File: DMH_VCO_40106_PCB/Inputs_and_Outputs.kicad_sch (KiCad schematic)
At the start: 9 parts, among them J1 Sync, J2 V/Oct, J3 Exp FM, J4 Lin FM, J5 PW Mod, J6 Senoid, J7 Triangle, J8 Square, J9 Sawtooth

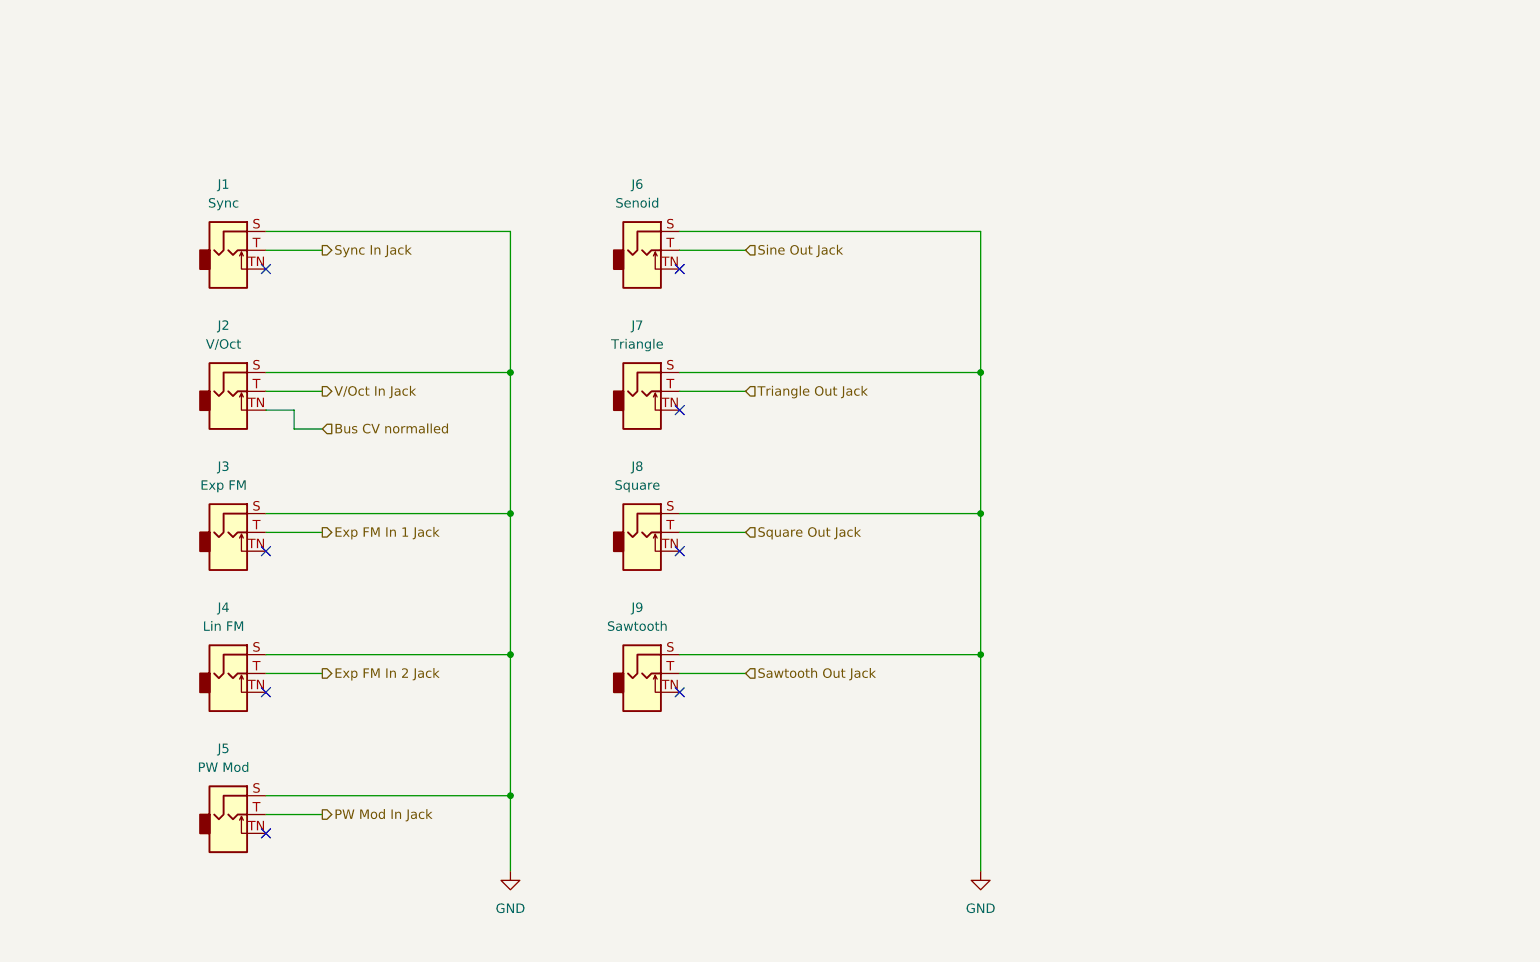
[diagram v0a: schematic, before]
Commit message: Added Sync and Bus CV switches
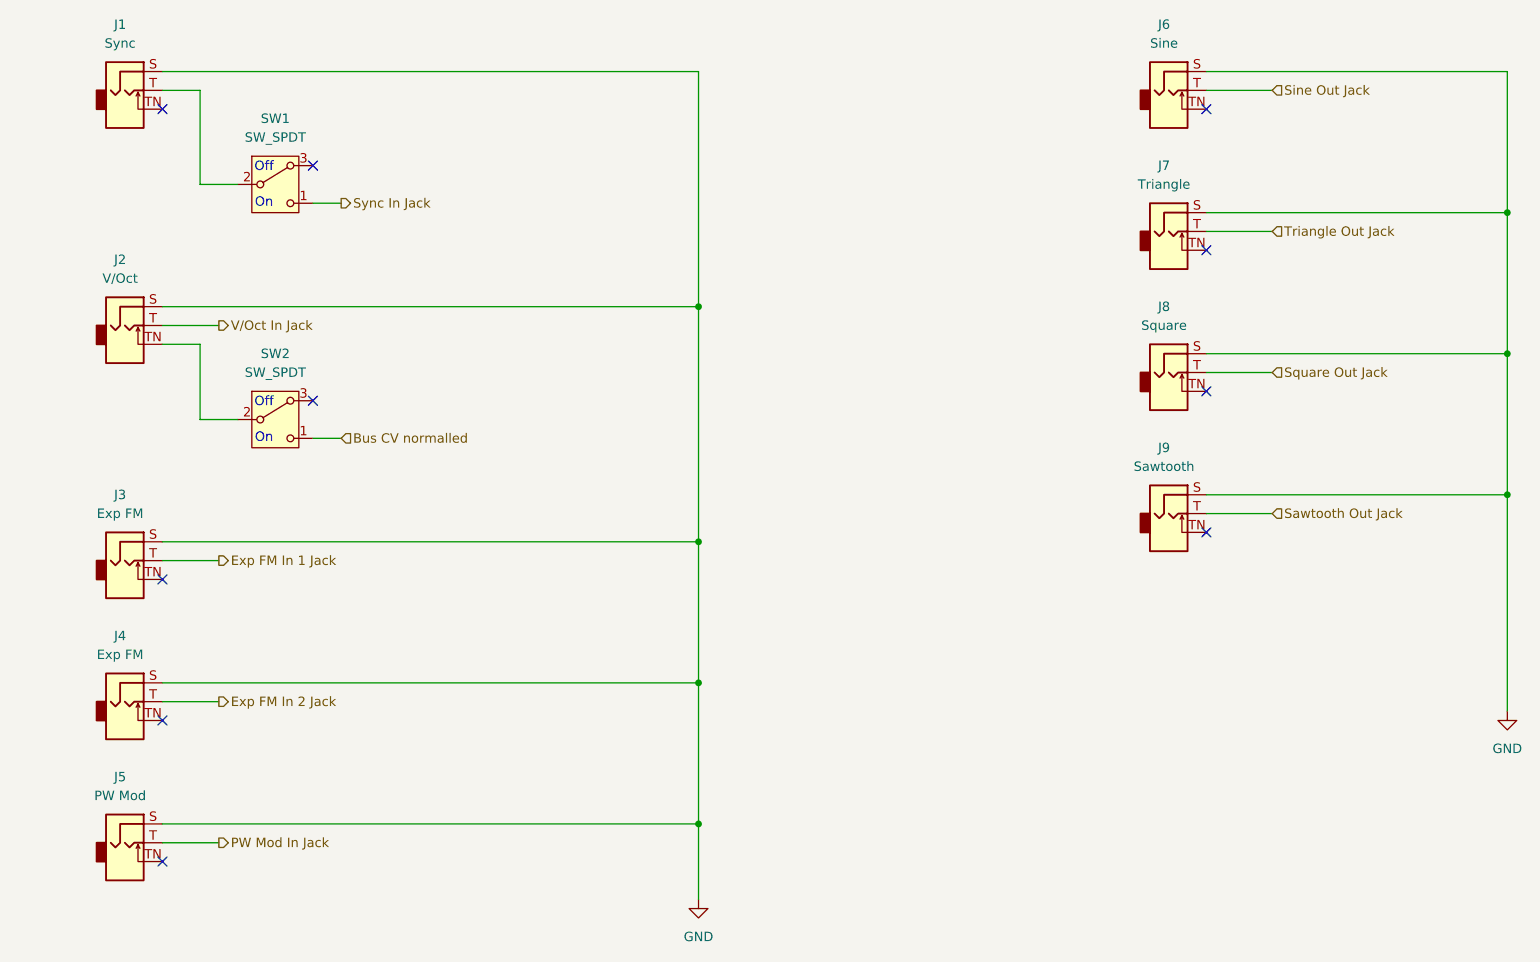
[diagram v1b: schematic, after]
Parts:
- added SW1, SW2: SW_SPDT, symbol Switch:SW_SPDT_321
- J4: value Lin FM -> Exp FM
- J6: value Senoid -> Sine
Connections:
- net Bus CV normalled: now also SW2.1 (C); no longer J2.TN
- net Sync In Jack: now also SW1.1 (C); no longer J1.T
- new net: J1.T, SW1.2 (B)
- new net: J2.TN, SW2.2 (B)
- no-connect marks 8 -> 10
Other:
- note added: "Off"
- note added: "On"
- moved on the sheet: J1, J2, J3, J4, J5, J6, J7, J8, J9

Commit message: Updated Tuner
- Changed uC to ATtiny4313
- Added LEDs
- Created "function" field and updated all jacks, switches and pots
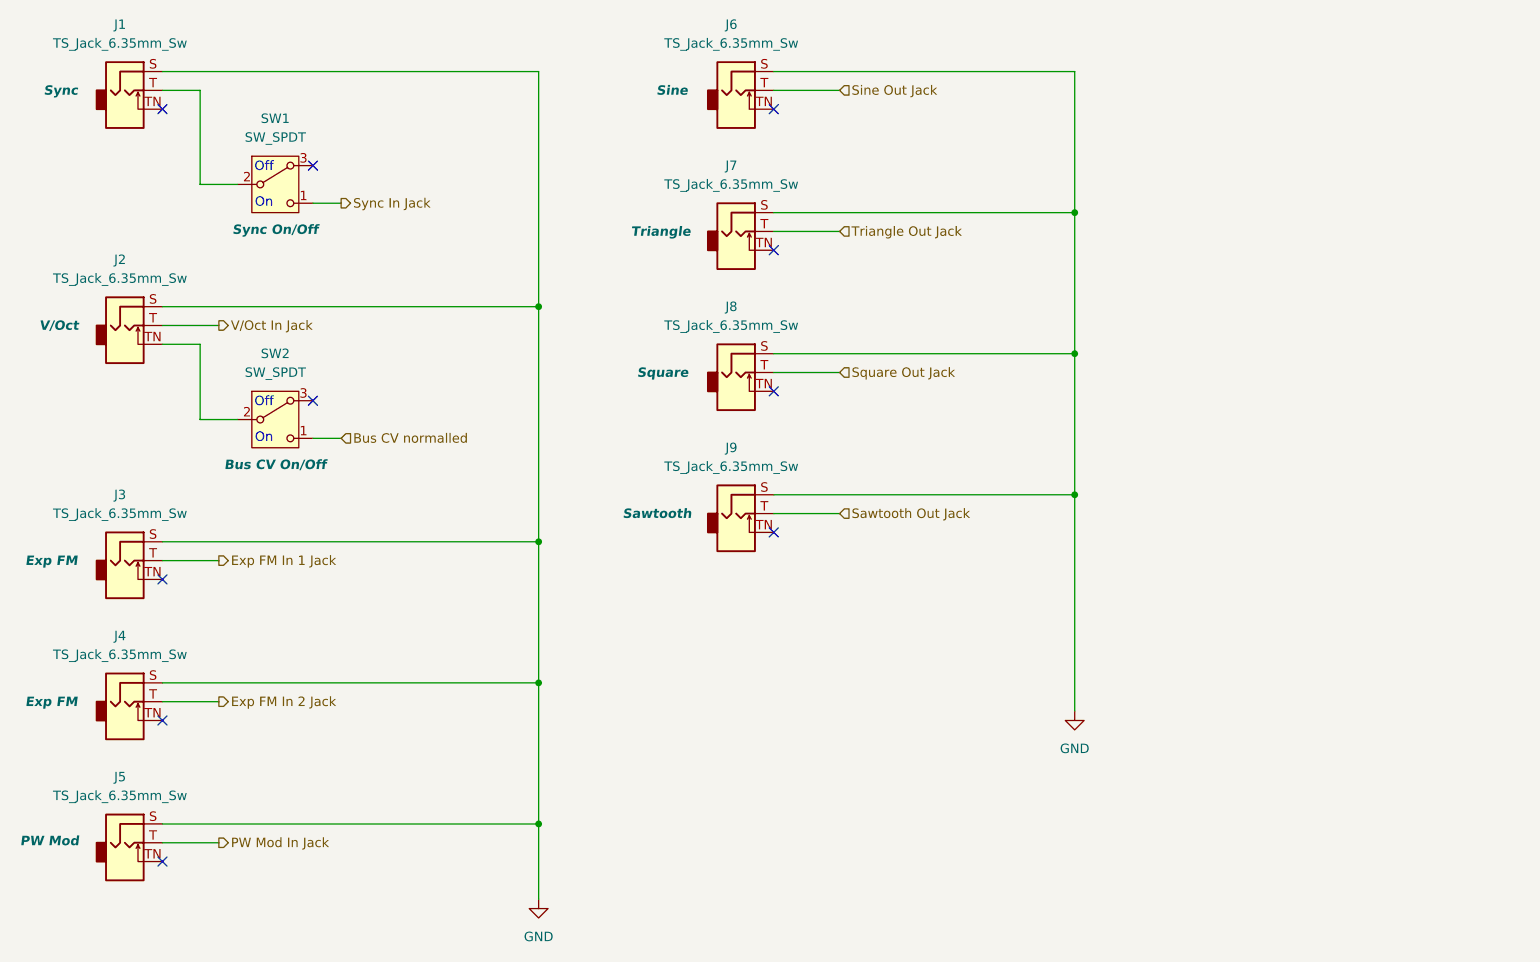
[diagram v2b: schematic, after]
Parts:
- J1: value Sync -> TS_Jack_6.35mm_Sw; Function (none) -> Sync
- J2: value V/Oct -> TS_Jack_6.35mm_Sw; Function (none) -> V/Oct
- J3, J4: value Exp FM -> TS_Jack_6.35mm_Sw; Function (none) -> Exp FM
- J5: value PW Mod -> TS_Jack_6.35mm_Sw; Function (none) -> PW Mod
- J6: value Sine -> TS_Jack_6.35mm_Sw; Function (none) -> Sine
- J7: value Triangle -> TS_Jack_6.35mm_Sw; Function (none) -> Triangle
- J8: value Square -> TS_Jack_6.35mm_Sw; Function (none) -> Square
- J9: value Sawtooth -> TS_Jack_6.35mm_Sw; Function (none) -> Sawtooth
- SW1: Function (none) -> Sync On/Off
- SW2: Function (none) -> Bus CV On/Off
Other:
- moved on the sheet: J6, J7, J8, J9
